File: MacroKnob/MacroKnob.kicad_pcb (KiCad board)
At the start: 2 copper layers, 14 parts, among them SW1 RotaryEncoder_Switch_MP, SW2 Up, SW3 Down, SW4 H, SW5 *, U2 Sparkfun_Pro_Micro

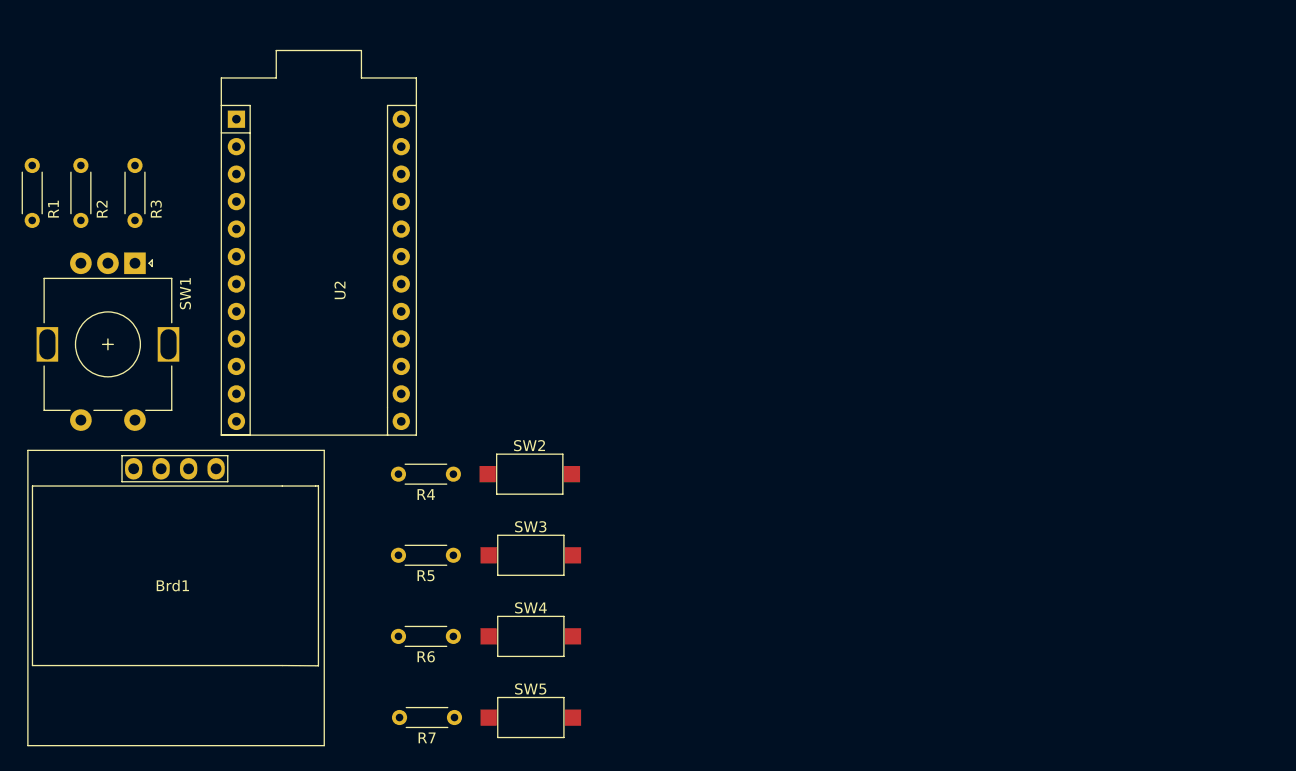
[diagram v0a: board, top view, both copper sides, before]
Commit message: Add Script for arduino
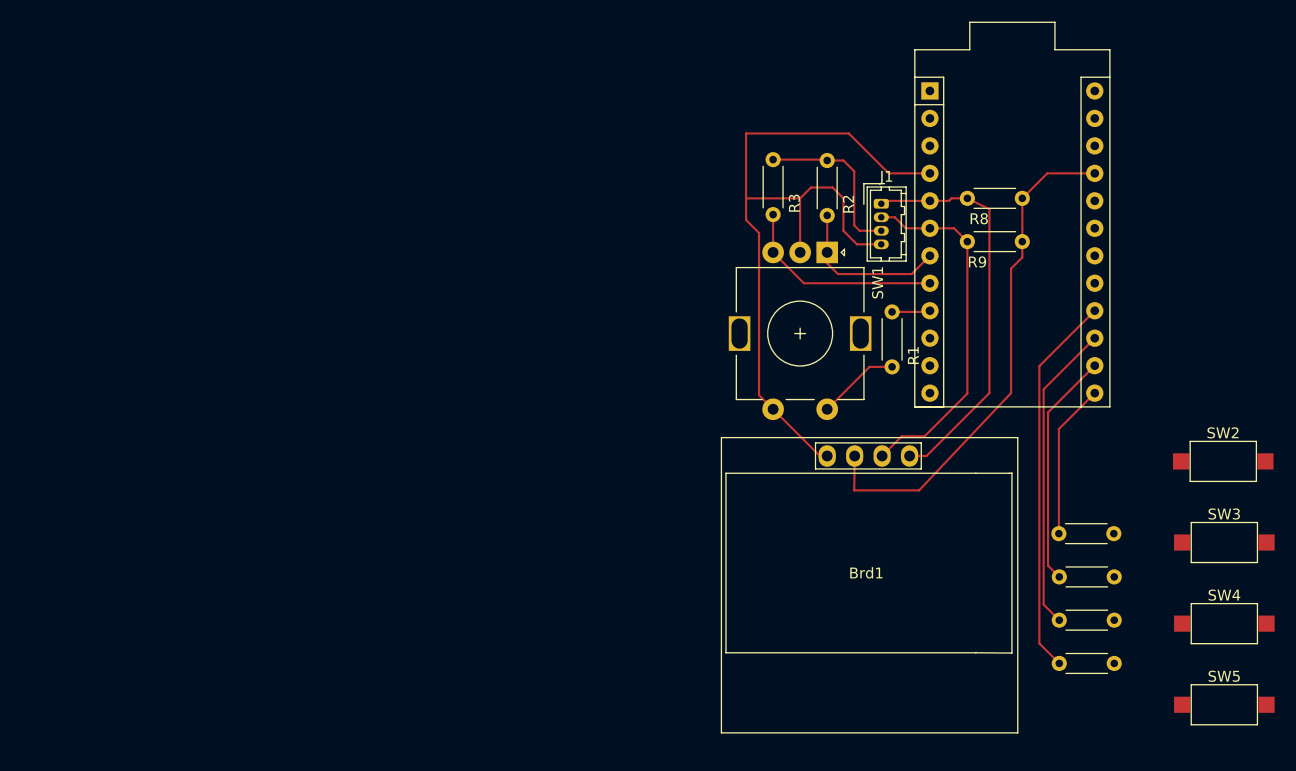
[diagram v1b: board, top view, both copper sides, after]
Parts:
- added J1: External I2C, Connector_Hirose:Hirose_DF13-04P-1.25DSA_1x04_P1.25mm_Vertical, F.Cu at (139.0, 74.5)
- added R8: 10K, Resistor_THT:R_Axial_DIN0204_L3.6mm_D1.6mm_P5.08mm_Horizontal, F.Cu at (152.0, 74.0)
- added R9: 10K, Resistor_THT:R_Axial_DIN0204_L3.6mm_D1.6mm_P5.08mm_Horizontal, F.Cu at (152.0, 78.0)
- SW1: value RotaryEncoder_Switch_MP -> RotaryEncoder
- moved R1 80.6 mm to (140.0, 84.5)
- moved R2 69.0 mm to (134.0, 70.5)
- moved U2 64.2 mm to (158.7, 92.0)
- moved Brd1 64.1 mm to (137.6, 108.4)
- moved SW2 64.1 mm to (170.6, 98.3)
- moved SW3 64.1 mm to (170.7, 105.8)
- moved SW4 64.1 mm to (170.7, 113.3)
- moved SW5 64.1 mm to (170.7, 120.8)
- moved SW1 64.0 mm to (134.0, 79.0)
- moved R4 61.3 mm to (160.5, 105.0)
- moved R7 61.2 mm to (160.5, 117.0)
- moved R5 61.1 mm to (160.5, 109.0)
- moved R6 61.1 mm to (160.5, 113.0)
- moved R3 59.0 mm to (129.0, 75.5)
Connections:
- Brd1 pad 1: unconnected-(Brd1-GND-Pad1) -> GND
- Brd1 pad 2: unconnected-(Brd1-VCC-Pad2) -> VCC
- Brd1 pad 3: unconnected-(Brd1-SCL-Pad3) -> SCL
- Brd1 pad 4: unconnected-(Brd1-SDA-Pad4) -> SDA
- R2 pad 1: VCC 5V -> VCC
- R3 pad 2: VCC 5V -> VCC
- R4 pad 2: unconnected-(R4-Pad2) -> Net-(U2-~D10/A10)
- R5 pad 2: unconnected-(R5-Pad2) -> Net-(U2-D16)
- R6 pad 2: unconnected-(R6-Pad2) -> Net-(U2-D14)
- R7 pad 2: unconnected-(R7-Pad2) -> Net-(U2-D15)
- SW1 pad A: CLK -> DT
- SW1 pad B: DT -> CLK
- SW1 pad S1: Net-(R1-Pad2) -> GND
- SW1 pad S2: GND -> Net-(R1-Pad2)
- U2 pad 13: unconnected-(U2-~D10/A10-Pad13) -> Net-(U2-~D10/A10)
- U2 pad 14: unconnected-(U2-D16-Pad14) -> Net-(U2-D16)
- U2 pad 15: unconnected-(U2-D14-Pad15) -> Net-(U2-D14)
- U2 pad 16: unconnected-(U2-D15-Pad16) -> Net-(U2-D15)
- U2 pad 21: unconnected-(U2-VCC-Pad21) -> VCC
- U2 pad 23: unconnected-(U2-GND-Pad23) -> GND
- U2 pad 5: unconnected-(U2-D2-Pad5) -> SDA
- U2 pad 6: unconnected-(U2-~D3-Pad6) -> SCL
- U2 pad 7: unconnected-(U2-D4/A6-Pad7) -> DT
- U2 pad 8: unconnected-(U2-~D5-Pad8) -> CLK
- U2 pad 9: unconnected-(U2-~D6/A7-Pad9) -> SW
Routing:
- net GND: track 0.00 -> 73.7 mm
- net VCC: track 0.00 -> 63.3 mm
- net SDA: track 0.00 -> 37.2 mm
- net Net-(U2-D15): track 0.00 -> 35.5 mm
- net SCL: track 0.00 -> 33.2 mm
- net Net-(U2-D14): track 0.00 -> 28.6 mm
- net Net-(U2-D16): track 0.00 -> 21.8 mm
- net CLK: track 0.00 -> 19.2 mm
- net DT: track 0.00 -> 15.0 mm
- net Net-(U2-~D10/A10): track 0.00 -> 14.4 mm
- net Net-(R1-Pad2): track 0.00 -> 7.62 mm
- net SW: track 0.00 -> 3.55 mm
